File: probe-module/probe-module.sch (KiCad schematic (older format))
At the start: 1 part

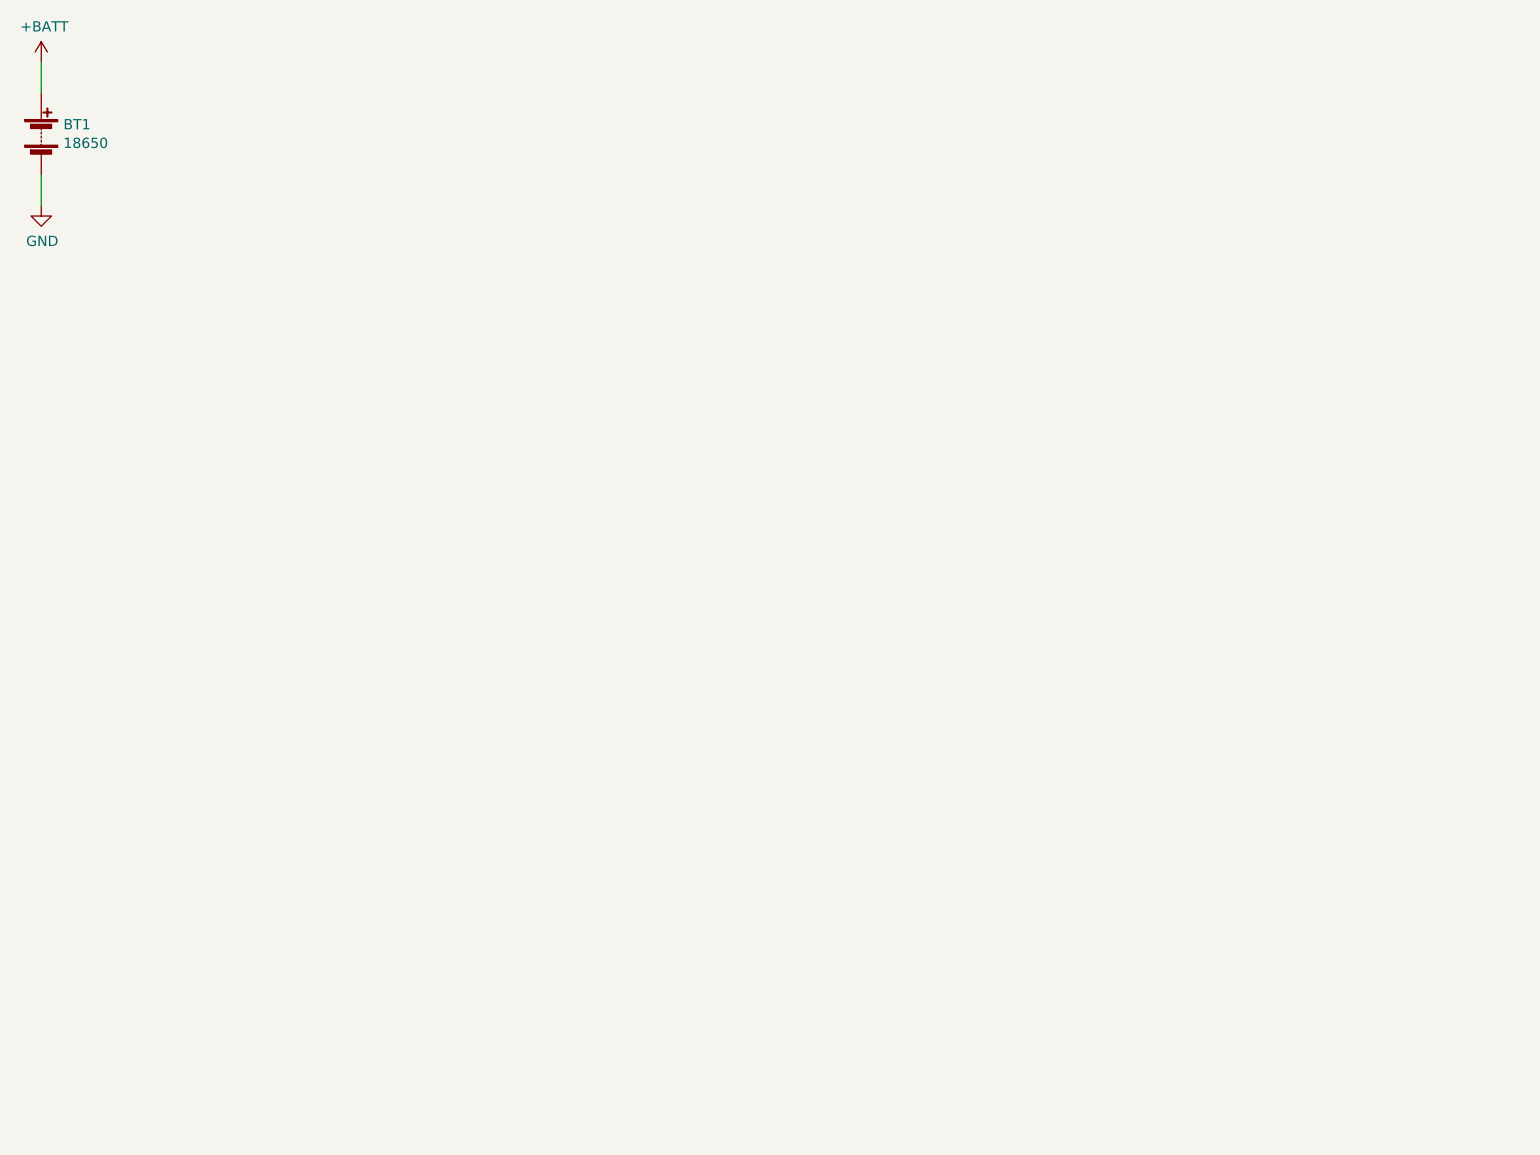
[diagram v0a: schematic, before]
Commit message: Fix too low net clearance
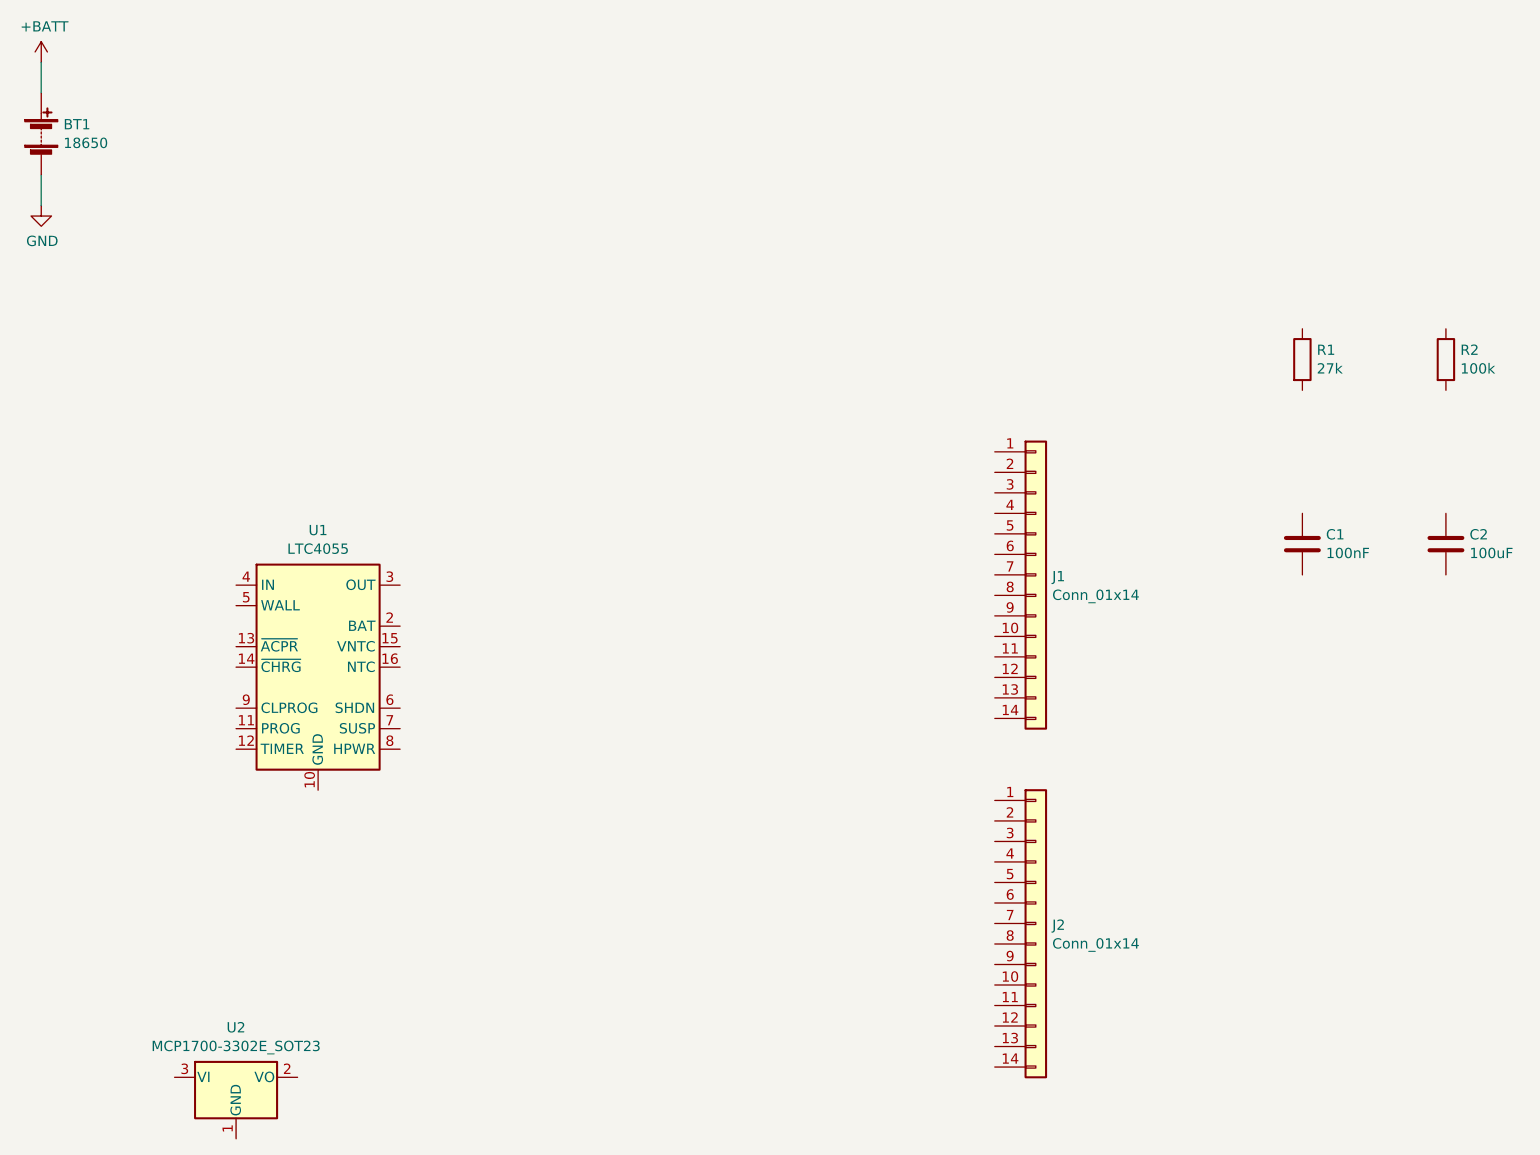
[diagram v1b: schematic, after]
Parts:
- added C1: 100nF, Capacitor_SMD:C_1206_3216Metric_Pad1.33x1.80mm_HandSolder, symbol Device:C
- added C2: 100uF, Capacitor_SMD:C_1206_3216Metric_Pad1.33x1.80mm_HandSolder, symbol Device:C
- added J1, J2: Conn_01x14, Connector_PinHeader_2.54mm:PinHeader_1x14_P2.54mm_Vertical, symbol Connector_Generic:Conn_01x14
- added R1: 27k, Resistor_SMD:R_1206_3216Metric_Pad1.30x1.75mm_HandSolder, symbol Device:R
- added R2: 100k, Resistor_SMD:R_1206_3216Metric_Pad1.30x1.75mm_HandSolder, symbol Device:R
- added U1: LTC4055, Package_DFN_QFN:QFN-16-1EP_4x4mm_P0.65mm_EP2.15x2.15mm, symbol Battery_Management:LTC4055
- added U2: MCP1700-3302E_SOT23, Package_TO_SOT_SMD:SOT-23, symbol Regulator_Linear:MCP1700-3302E_SOT23
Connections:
- new net: U1.1 (IN), U1.4 (IN)
- new net: U1.10 (GND), U1.17 (GND)
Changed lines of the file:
@@
 Wire Wire Line
 	1250 1600 1250 1750
+$Comp
+L Battery_Management:LTC4055 U1
+U 1 1 62BC203A
+P 2600 4000
+F 0 "U1" H 2600 4667 50  0000 C CNN
+F 1 "LTC4055" H 2600 4576 50  0000 C CNN
+F 2 "Package_DFN_QFN:QFN-16-1EP_4x4mm_P0.65mm_EP2.15x2.15mm" H 2600 3100 50  0001 C CNN
+F 3 "https://www.analog.com/media/en/technical-documentation/data-sheets/4055fb.pdf" H 2600 3500 50  0001 C CNN
+	1    2600 4000
+	1    0    0    -1
+$EndComp
+$Comp
+L Connector_Generic:Conn_01x14 J1
+U 1 1 62BC31FF
+P 6100 3550
+F 0 "J1" H 6180 3542 50  0000 L CNN
+F 1 "Conn_01x14" H 6180 3451 50  0000 L CNN
+F 2 "Connector_PinHeader_2.54mm:PinHeader_1x14_P2.54mm_Vertical" H 6100 3550 50  0001 C CNN
+F 3 "~" H 6100 3550 50  0001 C CNN
+	1    6100 3550
+	1    0    0    -1
+$EndComp
+$Comp
+L Connector_Generic:Conn_01x14 J2
+U 1 1 62BC3B30
+P 6100 5250
+F 0 "J2" H 6180 5242 50  0000 L CNN
+F 1 "Conn_01x14" H 6180 5151 50  0000 L CNN
+F 2 "Connector_PinHeader_2.54mm:PinHeader_1x14_P2.54mm_Vertical" H 6100 5250 50  0001 C CNN
+F 3 "~" H 6100 5250 50  0001 C CNN
+	1    6100 5250
+	1    0    0    -1
+$EndComp
+$Comp
+L Regulator_Linear:MCP1700-3302E_SOT23 U2
+U 1 1 62BC6C63
+P 2200 6000
+F 0 "U2" H 2200 6242 50  0000 C CNN
+F 1 "MCP1700-3302E_SOT23" H 2200 6151 50  0000 C CNN
+F 2 "Package_TO_SOT_SMD:SOT-23" H 2200 6225 50  0001 C CNN
+F 3 "http://ww1.microchip.com/downloads/en/DeviceDoc/20001826D.pdf" H 2200 6000 50  0001 C CNN
+	1    2200 6000
+	1    0    0    -1
+$EndComp
+$Comp
+L Device:R R1
+U 1 1 62BC7A1D
+P 7400 2500
+F 0 "R1" H 7470 2546 50  0000 L CNN
+F 1 "27k" H 7470 2455 50  0000 L CNN
+F 2 "Resistor_SMD:R_1206_3216Metric_Pad1.30x1.75mm_HandSolder" V 7330 2500 50  0001 C CNN
+F 3 "~" H 7400 2500 50  0001 C CNN
+	1    7400 2500
+	1    0    0    -1
+$EndComp
+$Comp
+L Device:R R2
+U 1 1 62BC88BA
+P 8100 2500
+F 0 "R2" H 8170 2546 50  0000 L CNN
+F 1 "100k" H 8170 2455 50  0000 L CNN
+F 2 "Resistor_SMD:R_1206_3216Metric_Pad1.30x1.75mm_HandSolder" V 8030 2500 50  0001 C CNN
+F 3 "~" H 8100 2500 50  0001 C CNN
+	1    8100 2500
+	1    0    0    -1
+$EndComp
+$Comp
+L Device:C C1
+U 1 1 62BC92F7
+P 7400 3400
+F 0 "C1" H 7515 3446 50  0000 L CNN
+F 1 "100nF" H 7515 3355 50  0000 L CNN
+F 2 "Capacitor_SMD:C_1206_3216Metric_Pad1.33x1.80mm_HandSolder" H 7438 3250 50  0001 C CNN
+F 3 "~" H 7400 3400 50  0001 C CNN
+	1    7400 3400
+	1    0    0    -1
+$EndComp
+$Comp
+L Device:C C2
+U 1 1 62BC986E
+P 8100 3400
+F 0 "C2" H 8215 3446 50  0000 L CNN
+F 1 "100uF" H 8215 3355 50  0000 L CNN
+F 2 "Capacitor_SMD:C_1206_3216Metric_Pad1.33x1.80mm_HandSolder" H 8138 3250 50  0001 C CNN
+F 3 "~" H 8100 3400 50  0001 C CNN
+	1    8100 3400
+	1    0    0    -1
+$EndComp
 $EndSCHEMATC
